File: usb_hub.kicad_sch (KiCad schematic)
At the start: 128 parts, among them J5 USB-C_Kycon_KUSBX-SL2-CS1N24-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, J6 USB-C_Kycon_KUSBX-SL2-CS1N24-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, Q21 DMC2400UV-7, Q26 DMC2400UV-7, Q27 DMC2400UV-7, Q29 DMC2400UV-7, U17 TPD4E05U06QDQARQ1, U18 AP22615A_TSOT26, U19 TPD4E05U06QDQARQ1, U20 AP22615A_TSOT26, U21 USB7252C, U24 TPD4E05U06QDQARQ1, U25 TPD4E05U06QDQARQ1, U27 TPD4E05U06QDQARQ1, U28 TPD4E05U06QDQARQ1, U52 SST26VF064B, Y2 Oscillator_25MHz_ESC_2016MV

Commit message: Update naming on schematic sheets and PCB, update release date
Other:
- title: Jetson AGX Thor Baseboard -> Antmicro Baseboard for Jetson AGX Thor
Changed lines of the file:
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@@
 	(paper "A3")
 	(title_block
-		(title "Jetson AGX Thor Baseboard")
-		(date "2025-11-03")
+		(title "Antmicro Baseboard for Jetson AGX Thor")
+		(date "2026-02-17")
 		(rev "1.1.0")
 		(company "Antmicro Ltd")

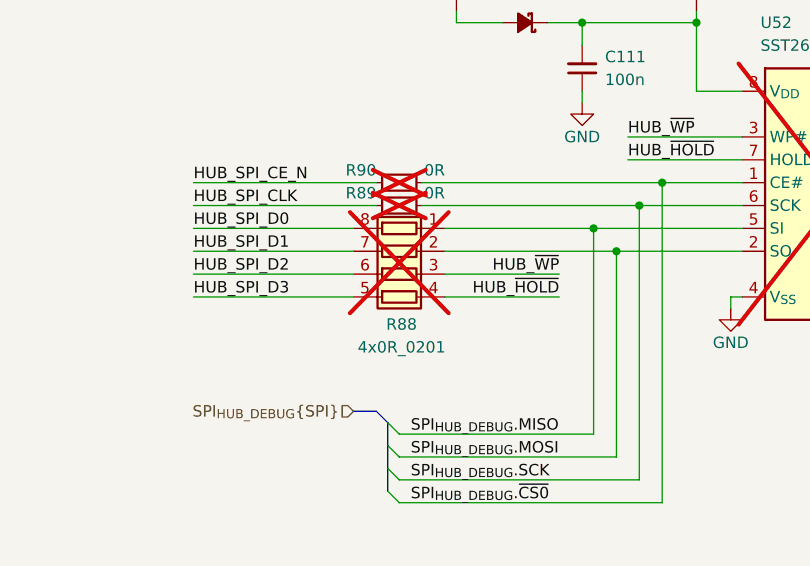
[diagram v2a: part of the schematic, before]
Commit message: [#88665] All Resistors array replaced by standalone resistors
Task done as described in #88665
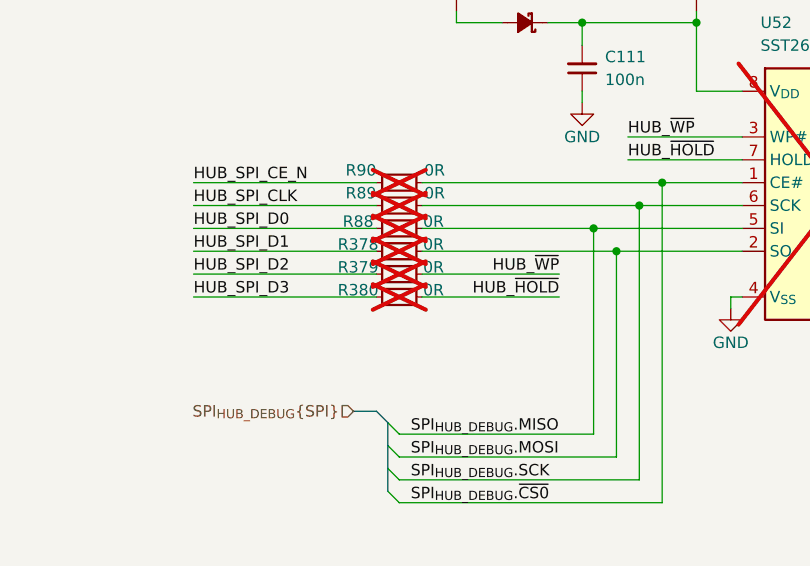
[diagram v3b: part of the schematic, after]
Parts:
- removed R88: R_4x0R_0201_array, antmicro-footprints:R_Array_4x0201_Panasonic_EXB18V, symbol antmicroResistorNetworksArrays:R_4x0R_0201_array
- added R378, R379, R380, R88: R_0R_0402, antmicro-footprints:R_0402_1005Metric, symbol antmicroResistors0402:R_0R_0402
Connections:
- net HUB_SPI_D0: now also R88.1
- net HUB_SPI_D1: now also R378.1
- net HUB_SPI_D2: now also R379.1
- net HUB_SPI_D3: now also R380.1
- net HUB_~{HOLD}: now also R380.2
- net HUB_~{WP}: now also R379.2
- net SPI_{HUB_DEBUG}.MISO: now also R88.2
- net SPI_{HUB_DEBUG}.MOSI: now also R378.2

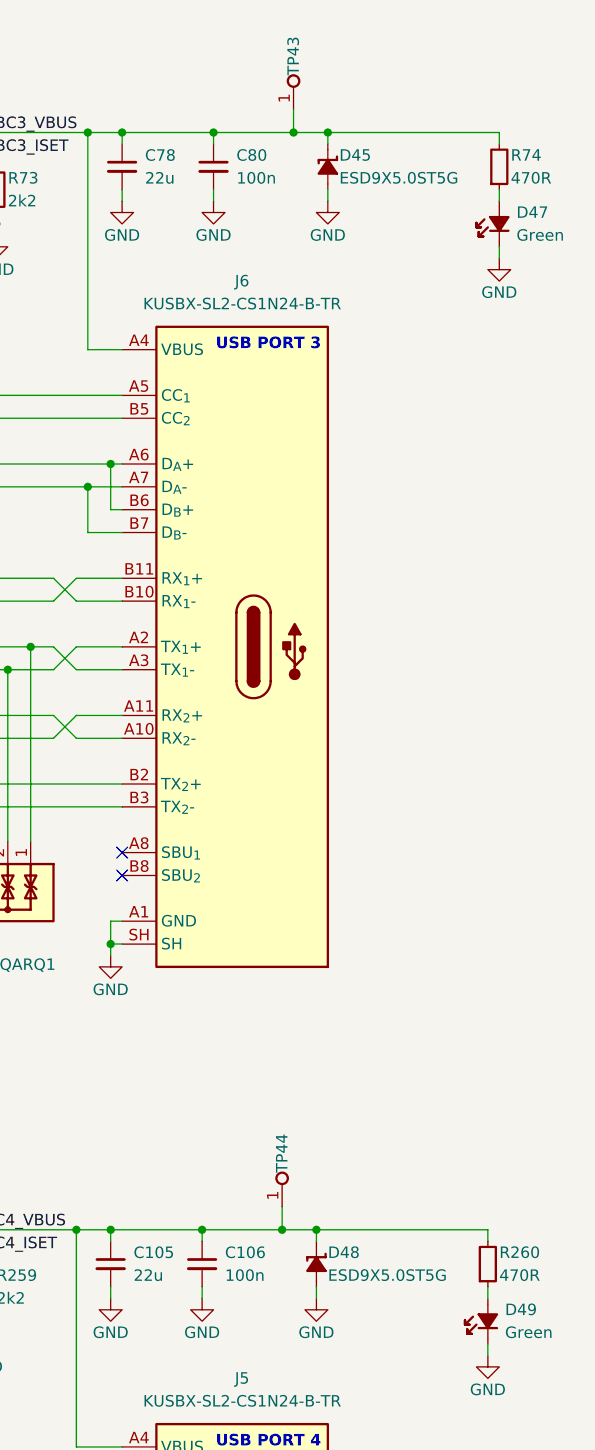
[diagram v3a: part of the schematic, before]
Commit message: [#88664] ESD9X5.0ST5G diodes replaced by PESD5Z5_0F, added TVS on Fan 12V
ESD9X5.0ST5G -> PESD5Z5_0F, changes done on schematics and PCB editor,
added TVS for fan 12V
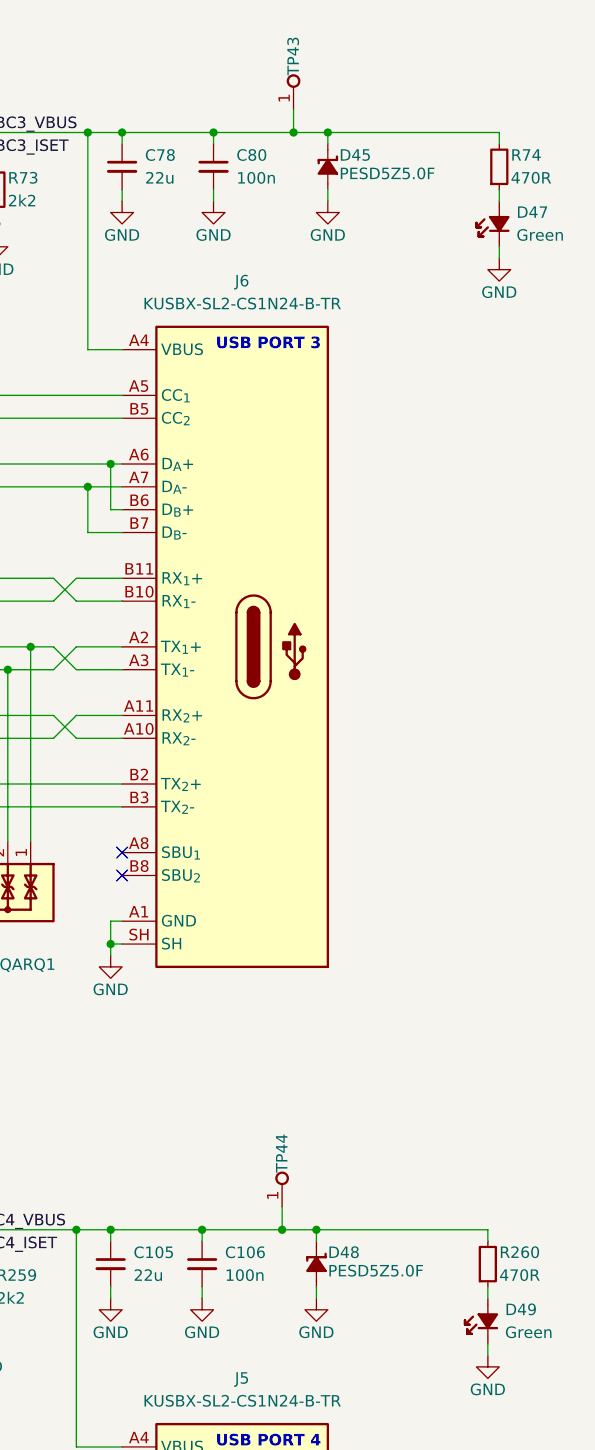
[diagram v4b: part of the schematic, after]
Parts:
- D45, D48: value ESD9X5.0ST5G -> PESD5Z5.0F; footprint antmicro-footprints:SOD-923 -> antmicro-footprints:SOD-523; symbol antmicroTVSDiodes:ESD9X5.0ST5G -> antmicroTVSDiodes:PESD5Z5_0F; MPN ESD9X5.0ST5G -> PESD5Z5.0F; Manufacturer ON Semiconductor -> Nexperia
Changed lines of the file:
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@@
 	)
 	(symbol
-		(lib_id "antmicroTVSDiodes:ESD9X5.0ST5G")
+		(lib_id "antmicroTVSDiodes:PESD5Z5_0F")
 		(at 374.65 33.02 270)
 		(unit 1)
@@
 			)
 		)
-		(property "Value" "ESD9X5.0ST5G"
+		(property "Value" "PESD5Z5.0F"
 			(at 359.41 54.61 0)
 			(effects
@@
 			)
 		)
-		(property "Footprint" "antmicro-footprints:SOD-923"
-			(at 367.03 54.61 0)
+		(property "Footprint" "antmicro-footprints:SOD-523"
+			(at 369.57 48.26 0)
 			(effects
 				(font
@@
 			)
 		)
-		(property "Datasheet" "https://www.onsemi.com/pdf/datasheet/esd9x3.3st5g-d.pdf"
-			(at 364.49 54.61 0)
+		(property "Datasheet" "https://assets.nexperia.com/documents/data-sheet/PESD5Z5_0.pdf"
+			(at 367.03 48.26 0)
 			(effects
 				(font
@@
 			)
 		)
-		(property "Description" "Unidirectional TVS, 30 kV,  SOD-923, 5 V, 65 pF"
-			(at 374.65 33.02 0)
+		(property "Description" "Unidirectional TVS, 30 kV,  SOD-523, 5 V, 89 pF"
+			(at 354.33 48.26 0)
 			(effects
 				(font
 					(size 1.27 1.27)
 				)
+				(justify left bottom)
 				(hide yes)
 			)
 		)
-		(property "Manufacturer" "ON Semiconductor"
-			(at 361.95 54.61 0)
+		(property "Manufacturer" "Nexperia"
+			(at 364.49 48.26 0)
 			(effects
 				(font
@@
 			)
 		)
-		(property "MPN" "ESD9X5.0ST5G"
-			(at 375.92 36.83 90)
+		(property "MPN" "PESD5Z5.0F"
+			(at 375.92 37.084 90)
 			(effects
 				(font
@@
 					(thickness 0.15)
 				)
-				(justify left)
+				(justify left bottom)
 			)
 		)
 		(property "Author" "Antmicro"
-			(at 356.87 54.61 0)
+			(at 359.41 48.26 0)
 			(effects
 				(font
@@
 		)
 		(property "License" "Apache-2.0"
-			(at 354.33 54.61 0)
+			(at 356.87 48.26 0)
 			(effects
 				(font
@@
 	)
 	(symbol
-		(lib_id "antmicroTVSDiodes:ESD9X5.0ST5G")
+		(lib_id "antmicroTVSDiodes:PESD5Z5_0F")
 		(at 373.38 154.94 270)
 		(unit 1)
@@
 			)
 		)
-		(property "Value" "ESD9X5.0ST5G"
+		(property "Value" "PESD5Z5.0F"
 			(at 358.14 176.53 0)
 			(effects
@@
 			)
 		)
-		(property "Footprint" "antmicro-footprints:SOD-923"
-			(at 365.76 176.53 0)
+		(property "Footprint" "antmicro-footprints:SOD-523"
+			(at 368.3 170.18 0)
 			(effects
 				(font
@@
 			)
 		)
-		(property "Datasheet" "https://www.onsemi.com/pdf/datasheet/esd9x3.3st5g-d.pdf"
-			(at 363.22 176.53 0)
+		(property "Datasheet" "https://assets.nexperia.com/documents/data-sheet/PESD5Z5_0.pdf"
+			(at 365.76 170.18 0)
 			(effects
 				(font
@@
 			)
 		)
-		(property "Description" "Unidirectional TVS, 30 kV,  SOD-923, 5 V, 65 pF"
-			(at 373.38 154.94 0)
+		(property "Description" "Unidirectional TVS, 30 kV,  SOD-523, 5 V, 89 pF"
+			(at 353.06 170.18 0)
 			(effects
 				(font
 					(size 1.27 1.27)
 				)
+				(justify left bottom)
 				(hide yes)
 			)
 		)
-		(property "Manufacturer" "ON Semiconductor"
-			(at 360.68 176.53 0)
+		(property "Manufacturer" "Nexperia"
+			(at 363.22 170.18 0)
 			(effects
 				(font
@@
 			)
 		)
-		(property "MPN" "ESD9X5.0ST5G"
-			(at 374.65 158.75 90)
+		(property "MPN" "PESD5Z5.0F"
+			(at 374.65 159.004 90)
 			(effects
 				(font
@@
 					(thickness 0.15)
 				)
-				(justify left)
+				(justify left bottom)
 			)
 		)
 		(property "Author" "Antmicro"
-			(at 355.6 176.53 0)
+			(at 358.14 170.18 0)
 			(effects
 				(font
@@
 		)
 		(property "License" "Apache-2.0"
-			(at 353.06 176.53 0)
+			(at 355.6 170.18 0)
 			(effects
 				(font

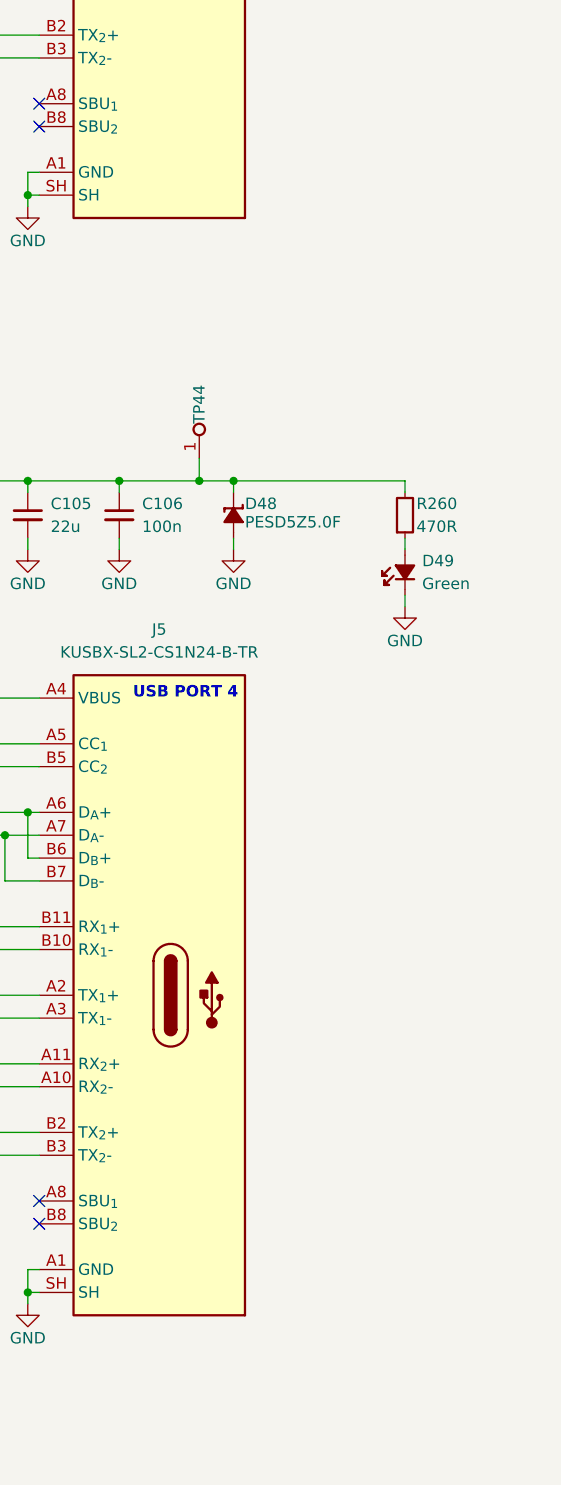
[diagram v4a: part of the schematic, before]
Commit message: [#89536] Add lightpipes for USB connectors LEDs
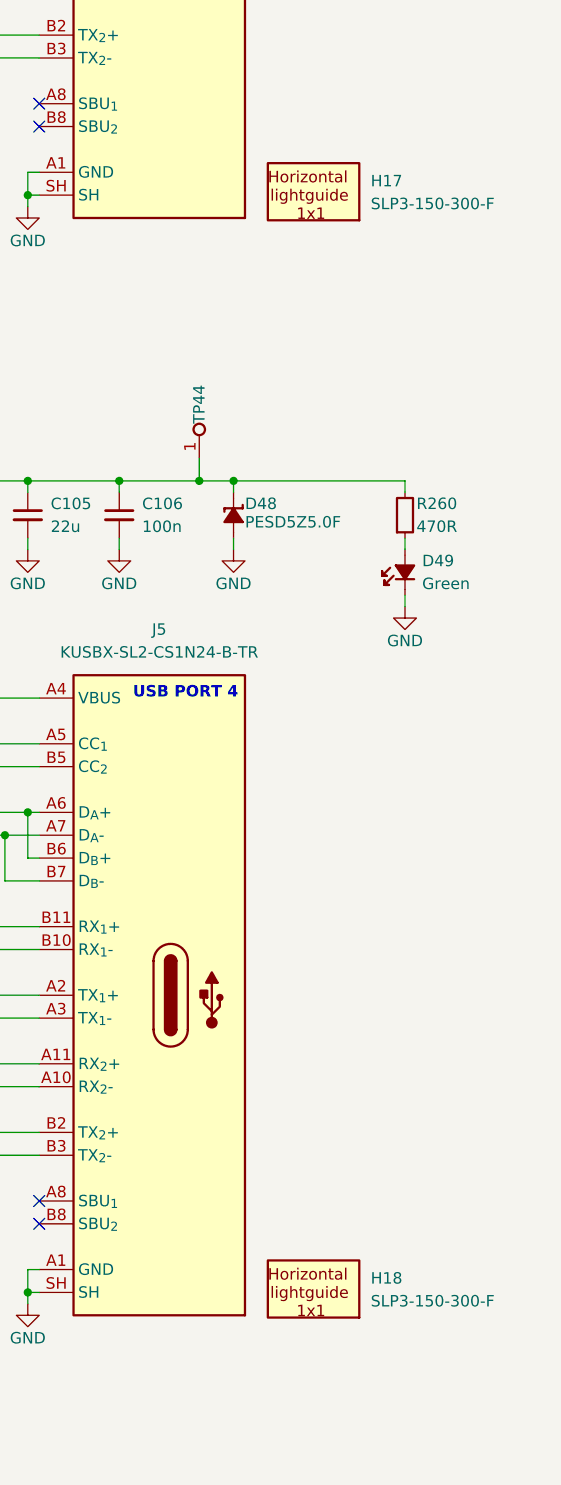
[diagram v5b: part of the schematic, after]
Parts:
- added H17, H18: Lightpipe_Bivar_SLP3-150-300-F, antmicro-footprints:Mech_Lightpipe_Bivar_SLP3-150-300-F, symbol antmicroMechanicalParts:Lightpipe_Bivar_SLP3-150-300-F
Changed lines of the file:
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@@
+	)
+	(symbol
+		(lib_id "antmicroMechanicalParts:Lightpipe_Bivar_SLP3-150-300-F")
+		(at 382.27 121.92 0)
+		(unit 1)
+		(exclude_from_sim no)
+		(in_bom yes)
+		(on_board yes)
+		(dnp no)
+		(fields_autoplaced yes)
+		(property "Reference" "H17"
+			(at 388.62 120.3517 0)
+			(effects
+				(font
+					(size 1.27 1.27)
+					(thickness 0.15)
+				)
+				(justify left)
+			)
+		)
+		(property "Value" "Lightpipe_Bivar_SLP3-150-300-F"
+			(at 394.03 129.235 0)
+			(effects
+				(font
+					(size 1.27 1.27)
+					(thickness 0.15)
+				)
+				(justify left bottom)
+				(hide yes)
+			)
+		)
+		(property "Footprint" "antmicro-footprints:Mech_Lightpipe_Bivar_SLP3-150-300-F"
+			(at 394.03 131.775 0)
+			(effects
+				(font
+					(size 1.27 1.27)
+					(thickness 0.15)
+				)
+				(justify left bottom)
+				(hide yes)
+			)
+		)
+		(property "Datasheet" "https://eu.mouser.com/datasheet/2/50/Bivar_SLP3_150_XXX_X_N-3318840.pdf"
+			(at 394.03 134.315 0)
+			(effects
+				(font
+					(size 1.27 1.27)
+					(thickness 0.15)
+				)
+				(justify left bottom)
+				(hide yes)
+			)
+		)
+		(property "Description" "LED Light Pipe, Rigid Board, Horizontal"
+			(at 394.03 144.475 0)
+			(effects
+				(font
+					(size 1.27 1.27)
+				)
+				(justify left bottom)
+				(hide yes)
+			)
+		)
+		(property "Manufacturer" "BIVAR"
+			(at 394.03 136.855 0)
+			(effects
+				(font
+					(size 1.27 1.27)
+					(thickness 0.15)
+				)
+				(justify left bottom)
+				(hide yes)
+			)
+		)
+		(property "MPN" "SLP3-150-300-F"
+			(at 388.62 122.8917 0)
+			(effects
+				(font
+					(size 1.27 1.27)
+					(thickness 0.15)
+				)
+				(justify left)
+			)
+		)
+		(property "Author" "Antmicro"
+			(at 394.03 139.395 0)
+			(effects
+				(font
+					(size 1.27 1.27)
+					(thickness 0.15)
+				)
+				(justify left bottom)
+				(hide yes)
+			)
+		)
+		(property "License" "Apache-2.0"
+			(at 394.03 141.935 0)
+			(effects
+				(font
+					(size 1.27 1.27)
+					(thickness 0.15)
+				)
+				(justify left bottom)
+				(hide yes)
+			)
+		)
+		(instances
+			(project "jetson-agx-thor-baseboard"
+				(path "/f569b0be-0afd-48b7-93ee-28582a4c645c/3fd0fbfa-9a42-4c7b-8c1c-08c3e88df372"
+					(reference "H17")
+					(unit 1)
+				)
+			)
+		)
 	)
 	(symbol
@@
 					(unit 1)
 				)
+			)
+		)
+	)
+	(symbol
+		(lib_id "antmicroMechanicalParts:Lightpipe_Bivar_SLP3-150-300-F")
+		(at 382.27 243.84 0)
+		(unit 1)
+		(exclude_from_sim no)
+		(in_bom yes)
+		(on_board yes)
+		(dnp no)
+		(fields_autoplaced yes)
+		(property "Reference" "H18"
+			(at 388.62 242.2717 0)
+			(effects
+				(font
+					(size 1.27 1.27)
+					(thickness 0.15)
+				)
+				(justify left)
+			)
+		)
+		(property "Value" "Lightpipe_Bivar_SLP3-150-300-F"
+			(at 394.03 251.155 0)
+			(effects
+				(font
+					(size 1.27 1.27)
+					(thickness 0.15)
+				)
+				(justify left bottom)
+				(hide yes)
+			)
+		)
+		(property "Footprint" "antmicro-footprints:Mech_Lightpipe_Bivar_SLP3-150-300-F"
+			(at 394.03 253.695 0)
+			(effects
+				(font
+					(size 1.27 1.27)
+					(thickness 0.15)
+				)
+				(justify left bottom)
+				(hide yes)
+			)
+		)
+		(property "Datasheet" "https://eu.mouser.com/datasheet/2/50/Bivar_SLP3_150_XXX_X_N-3318840.pdf"
+			(at 394.03 256.235 0)
+			(effects
+				(font
+					(size 1.27 1.27)
+					(thickness 0.15)
+				)
+				(justify left bottom)
+				(hide yes)
+			)
+		)
+		(property "Description" "LED Light Pipe, Rigid Board, Horizontal"
+			(at 394.03 266.395 0)
+			(effects
+				(font
+					(size 1.27 1.27)
+				)
+				(justify left bottom)
+				(hide yes)
+			)
+		)
+		(property "Manufacturer" "BIVAR"
+			(at 394.03 258.775 0)
+			(effects
+				(font
+					(size 1.27 1.27)
+					(thickness 0.15)
+				)
+				(justify left bottom)
+				(hide yes)
+			)
+		)
+		(property "MPN" "SLP3-150-300-F"
+			(at 388.62 244.8117 0)
+			(effects
+				(font
+					(size 1.27 1.27)
+					(thickness 0.15)
+				)
+				(justify left)
+			)
+		)
+		(property "Author" "Antmicro"
+			(at 394.03 261.315 0)
+			(effects
+				(font
+					(size 1.27 1.27)
+					(thickness 0.15)
+				)
+				(justify left bottom)
+				(hide yes)
+			)
+		)
+		(property "License" "Apache-2.0"
+			(at 394.03 263.855 0)
+			(effects
+				(font
+					(size 1.27 1.27)
+					(thickness 0.15)
+				)
+				(justify left bottom)
+				(hide yes)
+			)
+		)
+		(instances
+			(project "jetson-agx-thor-baseboard"
+				(path "/f569b0be-0afd-48b7-93ee-28582a4c645c/3fd0fbfa-9a42-4c7b-8c1c-08c3e88df372"
+					(reference "H18")
+					(unit 1)
+				)
